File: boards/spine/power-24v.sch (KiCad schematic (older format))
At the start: 0 parts

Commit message: Power management and such
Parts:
- added C72: 0.1uF, 0805, symbol C
- added C73: 1uF, 0805, symbol C
- added CON1: 5-24V 5A, symbol BARREL_JACK
- added CON2: 5-24V 16A, symbol CONN_01X04
- added D8: 8.5VWM, symbol D_Schottky_x2_ACom_KKA
- added Q4: AOD4189, TO-252, symbol Q_PMOS_GDS
- added R33: 100k, symbol R
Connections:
- new net: C72.2, CON1.1, CON2.1 (P1), CON2.2 (P2), Q4.2 (D)
- new net: D8.3 (A), Q4.1 (G), R33.1
- new net +24V: C73.1, D8.1 (K), D8.2 (K), Q4.3 (S)
- new net GND: C72.1, C73.2, CON1.2, CON1.3, CON2.3 (P3), CON2.4 (P4), R33.2
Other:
- note added: "Power input options"
- note added: "Reverse polarity protection"
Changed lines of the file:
@@
 Comment4 ""
 $EndDescr
+$Comp
+L +24V #PWR0138
+U 1 1 564D5D45
+P 7550 3250
+F 0 "#PWR0138" H 7550 3100 50  0001 C CNN
+F 1 "+24V" H 7550 3390 50  0000 C CNN
+F 2 "" H 7550 3250 60  0000 C CNN
+F 3 "" H 7550 3250 60  0000 C CNN
+	1    7550 3250
+	1    0    0    -1
+$EndComp
+$Comp
+L GNDPWR #PWR0139
+U 1 1 564D5D5C
+P 7100 5000
+F 0 "#PWR0139" H 7100 4800 50  0001 C CNN
+F 1 "GNDPWR" H 7100 4870 50  0000 C CNN
+F 2 "" H 7100 4950 60  0000 C CNN
+F 3 "" H 7100 4950 60  0000 C CNN
+	1    7100 5000
+	1    0    0    -1
+$EndComp
+$Comp
+L C C73
+U 1 1 564D690E
+P 7550 4100
+F 0 "C73" H 7600 4200 50  0000 L CNN
+F 1 "1uF " H 7600 4000 50  0000 L CNN
+F 2 "0805" H 7588 3950 30  0001 C CNN
+F 3 "http://www.murata.com/~/media/webrenewal/support/library/catalog/products/capacitor/mlcc/c02e.ashx" H 7550 4100 60  0001 C CNN
+F 4 "GRM219R61H105KA73D" H 7600 3900 39  0001 L BNN "MfgId"
+F 5 "Murata" H 7550 4100 60  0001 C CNN "MfrId"
+F 6 "Digikey" H 7550 4100 60  0001 C CNN "Vend1"
+F 7 "490-10743-2-ND" H 7550 4100 60  0001 C CNN "Vend1Id"
+F 8 "0.03980" H 7550 4100 60  0001 C CNN "RefPrice1k"
+	1    7550 4100
+	1    0    0    -1
+$EndComp
+$Comp
+L GND #PWR0140
+U 1 1 564D690F
+P 7550 5000
+F 0 "#PWR0140" H 7550 4750 50  0001 C CNN
+F 1 "GND" H 7550 4850 50  0000 C CNN
+F 2 "" H 7550 5000 60  0000 C CNN
+F 3 "" H 7550 5000 60  0000 C CNN
+	1    7550 5000
+	1    0    0    -1
+$EndComp
+$Comp
+L BARREL_JACK CON1
+U 1 1 564D6BF2
+P 3950 4050
+F 0 "CON1" H 3950 4300 60  0000 C CNN
+F 1 "5-24V 5A" H 3950 3850 60  0000 C CNN
+F 2 "" H 3950 4050 60  0000 C CNN
+F 3 "http://katalog.we-online.de/em/datasheet/6941xx105102.pdf" H 3950 4050 60  0001 C CNN
+F 4 "Digikey" H 3950 4050 60  0001 C CNN "Vend1"
+F 5 "732-5932-1-ND" H 3950 4050 60  0001 C CNN "Vend1Id"
+F 6 "Wurth" H 3950 4050 60  0001 C CNN "MfrId"
+F 7 "694108105102" H 3950 4050 60  0001 C CNN "MfgId"
+F 8 "1.13" H 3950 4050 60  0001 C CNN "RefPrice1k"
+	1    3950 4050
+	1    0    0    -1
+$EndComp
+$Comp
+L Q_PMOS_GDS Q4
+U 1 1 564D73AF
+P 6050 3500
+F 0 "Q4" V 6300 3750 50  0000 R CNN
+F 1 "AOD4189" V 6300 3550 50  0000 R CNN
+F 2 "TO-252" H 6250 3600 29  0001 C CNN
+F 3 "http://aosmd.com/res/data_sheets/AOD4189.pdf" H 6050 3500 60  0001 C CNN
+F 4 "Digikey" H 6050 3500 60  0001 C CNN "Vend1"
+F 5 "785-1351-1-ND" H 6050 3500 60  0001 C CNN "Vend1Id"
+F 6 "Alpha & Omega" H 6050 3500 60  0001 C CNN "MfgId"
+F 7 "AOD4189" H 6050 3500 60  0001 C CNN "MfrId"
+F 8 "0.196" H 6050 3500 60  0001 C CNN "RefPrice1k"
+	1    6050 3500
+	0    -1   -1   0
+$EndComp
+Wire Wire Line
+	4550 3400 5850 3400
+$Comp
+L C C72
+U 1 1 564D7783
+P 5700 4100
+F 0 "C72" V 5750 3900 50  0000 L CNN
+F 1 "0.1uF" V 5750 4200 50  0000 L CNN
+F 2 "0805" H 5738 3950 30  0001 C CNN
+F 3 "http://psearch.murata.com/capacitor/product/GRM21BR71H104MA01%23.pdf" H 5700 4100 60  0001 C CNN
+F 4 "0.01880" V 5700 4100 60  0001 C CNN "RefPrice1k"
+F 5 "490-9672-2-ND" V 5700 4100 60  0001 C CNN "Vend1Id"
+F 6 "Digikey" V 5700 4100 60  0001 C CNN "Vend1"
+F 7 "Murata" V 5700 4100 60  0001 C CNN "MfrId"
+F 8 "GRM21BR71H104MA01L" V 5700 4100 60  0001 C CNN "MfgId"
+	1    5700 4100
+	-1   0    0    1
+$EndComp
+Wire Wire Line
+	4550 4850 7550 4850
+Wire Wire Line
+	5700 3950 5700 3400
+Connection ~ 5700 3400
+Wire Wire Line
+	5700 4250 5700 4850
+Connection ~ 5700 4850
+$Comp
+L CONN_01X04 CON2
+U 1 1 564D79D9
+P 5150 4100
+F 0 "CON2" H 5150 4350 50  0000 C CNN
+F 1 "5-24V 16A" H 5050 3800 50  0000 C CNN
+F 2 "" H 5150 4100 60  0000 C CNN
+F 3 "http://www.diytrade.com/china/pd/11802786/terminal_block_2EDG_5_08_2P_3P_4P_5P_6P_7P_8P_9P_10P_11P_12P_13P_14P.html" H 5150 4100 60  0001 C CNN
+F 4 "eBay" H 5150 4100 60  0001 C CNN "Vend1"
+F 5 "http://www.ebay.com/itm/331290774584" H 5150 4100 60  0001 C CNN "Vend1Id"
+F 6 "0.23" H 5150 4100 60  0001 C CNN "RefPrice1k"
+F 7 "4way 4pin Screw PCB Terminal Block Connector 3.81mm Pitch Pluggable Type" H 5150 4100 60  0001 C CNN "Description"
+F 8 "E-xun" H 5150 4100 60  0001 C CNN "MfrId"
+F 9 "2EDG-3.81" H 5150 4100 60  0001 C CNN "MfgId"
+	1    5150 4100
+	1    0    0    -1
+$EndComp
+Wire Wire Line
+	4250 3950 4950 3950
+Wire Wire Line
+	4950 4050 4850 4050
+Wire Wire Line
+	4850 4050 4850 3950
+Connection ~ 4850 3950
+Wire Wire Line
+	4250 4050 4300 4050
+Wire Wire Line
+	4300 4050 4300 4150
+Wire Wire Line
+	4250 4150 4950 4150
+Connection ~ 4300 4150
+Wire Wire Line
+	4950 4250 4850 4250
+Wire Wire Line
+	4850 4250 4850 4150
+Connection ~ 4850 4150
+Text Notes 6000 2950 0    60   ~ 0
+Reverse polarity protection
+Text Notes 4050 2950 0    60   ~ 0
+Power input options
+$Comp
+L D_Schottky_x2_ACom_KKA D8
+U 1 1 564D8C89
+P 6800 3800
+F 0 "D8" H 7000 4000 50  0000 R CNN
+F 1 "8.5VWM" H 6550 4000 50  0000 L CNN
+F 2 "" H 6800 3800 60  0000 C CNN
+F 3 "http://www.onsemi.com/pub_link/Collateral/MMBZ5V6ALT1-D.PDF" H 6800 3800 60  0001 C CNN
+F 4 "ON Semi" H 6450 3950 39  0001 L BNN "MfrId"
+F 5 "MMBZ12VALT1G" H 6800 3900 39  0000 C CNN "MfgId"
+F 6 "MMBZ12VALT1GOSCT-ND" H 6800 3800 60  0001 C CNN "Vend1Id"
+F 7 ".04471" H 6800 3800 60  0001 C CNN "RefPrice1k"
+F 8 "Digikey" H 6800 3800 60  0001 C CNN "Vend1"
+	1    6800 3800
+	1    0    0    -1
+$EndComp
+$Comp
+L R R33
+U 1 1 564DB940
+P 6050 4400
+F 0 "R33" V 6130 4400 50  0000 C CNN
+F 1 "100k" V 6050 4400 50  0000 C CNN
+F 2 "" V 5980 4400 30  0000 C CNN
+F 3 "https://www.seielect.com/Catalog/SEI-RMCF_RMCP.pdf" H 6050 4400 30  0001 C CNN
+F 4 "Digikey" V 6050 4400 60  0001 C CNN "Vend1"
+F 5 "Stackpole" V 6050 4400 60  0001 C CNN "MfrId"
+F 6 "RMCF0805JT100K" V 6050 4400 60  0001 C CNN "MfgId"
+F 7 "RMCF0805JT100KCT-ND" V 6050 4400 60  0001 C CNN "Vend1Id"
+F 8 "0.00320" V 6050 4400 60  0001 C CNN "RefPrice1k"
+	1    6050 4400
+	1    0    0    -1
+$EndComp
+Connection ~ 6050 4850
+Wire Wire Line
+	4550 3400 4550 3950
+Connection ~ 4550 3950
+Wire Wire Line
+	4550 4150 4550 4850
+Connection ~ 4550 4150
+Wire Wire Line
+	6250 3400 7550 3400
+Wire Wire Line
+	7250 3400 7250 3800
+Wire Wire Line
+	7250 3800 7100 3800
+Wire Wire Line
+	6500 3800 6350 3800
+Wire Wire Line
+	6350 3800 6350 3400
+Connection ~ 6350 3400
+Wire Wire Line
+	6800 4000 6800 4100
+Wire Wire Line
+	6800 4100 6050 4100
+Wire Wire Line
+	6050 3700 6050 4250
+Connection ~ 6050 4100
+Wire Wire Line
+	6050 4550 6050 4850
+Wire Wire Line
+	7550 3250 7550 3950
+Wire Wire Line
+	7550 4250 7550 5000
+Connection ~ 7550 3400
+Connection ~ 7250 3400
+Connection ~ 7550 4850
+Wire Wire Line
+	7100 5000 7100 4850
+Connection ~ 7100 4850
 $EndSCHEMATC

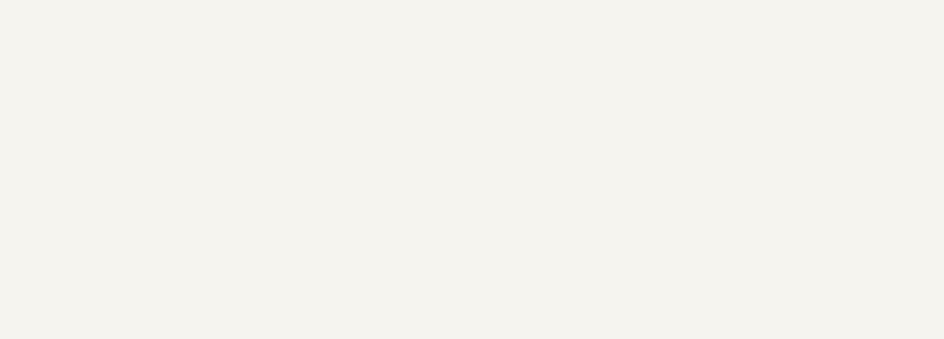
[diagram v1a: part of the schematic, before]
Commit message: Clock generator, sync connectors, title blocks
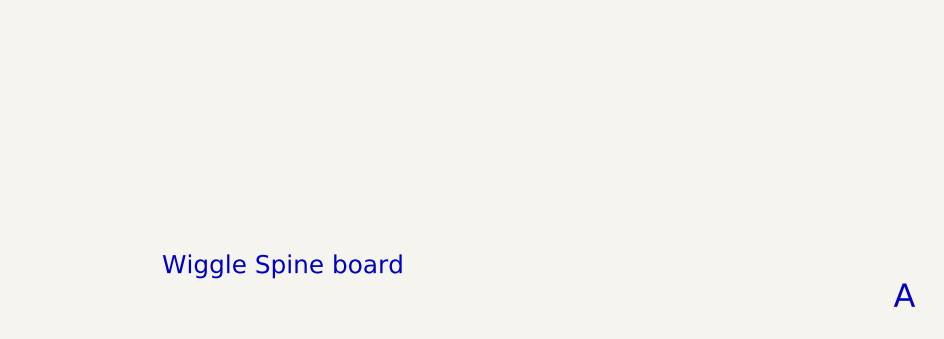
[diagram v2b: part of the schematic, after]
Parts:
- C72, C73: footprint 0805 -> Capacitors_SMD:C_0805
- R33: footprint (none) -> Resistors_SMD:R_0805
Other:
- note added: "A"
- note added: "Wiggle Spine board"

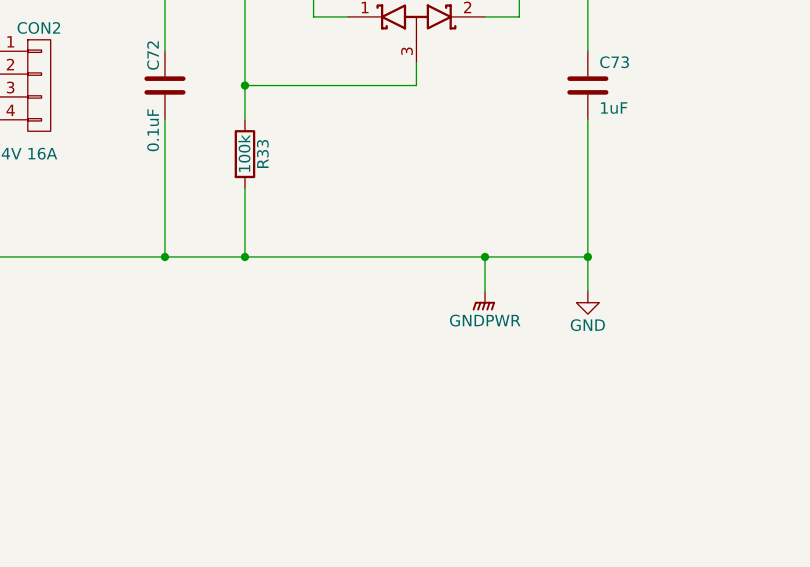
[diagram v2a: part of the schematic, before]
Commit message: Fixes for shield grounds and module numbering
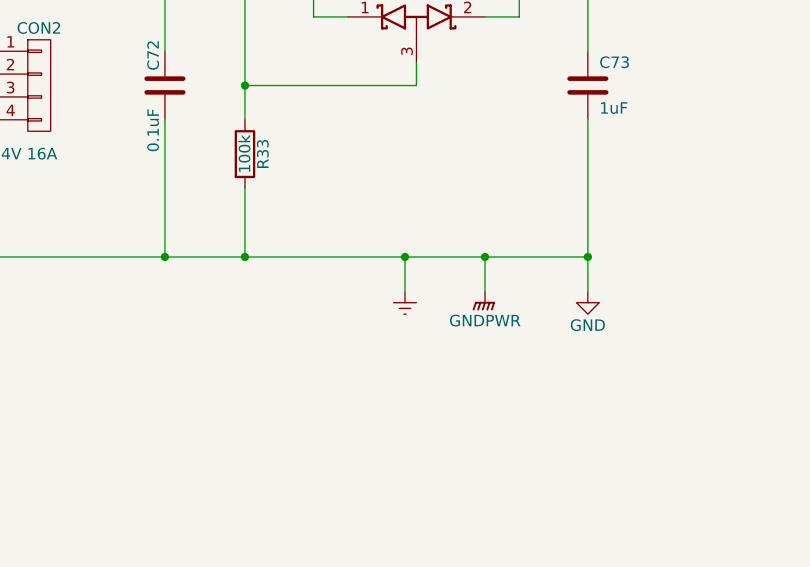
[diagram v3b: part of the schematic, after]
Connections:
- net GND renamed Earth
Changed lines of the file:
@@
 $EndDescr
 $Comp
-L +24V #PWR0138
+L +24V #PWR0139
 U 1 1 564D5D45
 P 7550 3250
-F 0 "#PWR0138" H 7550 3100 50  0001 C CNN
+F 0 "#PWR0139" H 7550 3100 50  0001 C CNN
 F 1 "+24V" H 7550 3390 50  0000 C CNN
 F 2 "" H 7550 3250 60  0000 C CNN
@@
 $EndComp
 $Comp
-L GNDPWR #PWR0139
+L GNDPWR #PWR0140
 U 1 1 564D5D5C
 P 7100 5000
-F 0 "#PWR0139" H 7100 4800 50  0001 C CNN
+F 0 "#PWR0140" H 7100 4800 50  0001 C CNN
 F 1 "GNDPWR" H 7100 4870 50  0000 C CNN
 F 2 "" H 7100 4950 60  0000 C CNN
@@
 $EndComp
 $Comp
-L GND #PWR0140
+L GND #PWR0141
 U 1 1 564D690F
 P 7550 5000
-F 0 "#PWR0140" H 7550 4750 50  0001 C CNN
+F 0 "#PWR0141" H 7550 4750 50  0001 C CNN
 F 1 "GND" H 7550 4850 50  0000 C CNN
 F 2 "" H 7550 5000 60  0000 C CNN
@@
 Text Notes 9900 7900 0    102  ~ 0
 A
+$Comp
+L Earth #PWR0142
+U 1 1 565B7572
+P 6750 5000
+F 0 "#PWR0142" H 6750 4750 50  0001 C CNN
+F 1 "Earth" H 6750 4850 50  0001 C CNN
+F 2 "" H 6750 5000 60  0000 C CNN
+F 3 "" H 6750 5000 60  0000 C CNN
+	1    6750 5000
+	1    0    0    -1
+$EndComp
+Wire Wire Line
+	6750 5000 6750 4850
+Connection ~ 6750 4850
 $EndSCHEMATC

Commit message: Schematic footprint and refdes work
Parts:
- CON1: footprint (none) -> Connect:BARREL_JACK
- CON2: footprint (none) -> Terminal_Blocks:TerminalBlock_Pheonix_PT-3.5mm_4pol
- D8: footprint (none) -> TO_SOT_Packages_SMD:SOT-23
- Q4: footprint TO-252 -> TO_SOT_Packages_SMD:TO-252-2Lead
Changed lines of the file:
@@
 $EndDescr
 $Comp
-L +24V #PWR0139
+L +24V #PWR141
 U 1 1 564D5D45
 P 7550 3250
-F 0 "#PWR0139" H 7550 3100 50  0001 C CNN
+F 0 "#PWR141" H 7550 3100 50  0001 C CNN
 F 1 "+24V" H 7550 3390 50  0000 C CNN
 F 2 "" H 7550 3250 60  0000 C CNN
@@
 $EndComp
 $Comp
-L GNDPWR #PWR0140
+L GNDPWR #PWR140
 U 1 1 564D5D5C
 P 7100 5000
-F 0 "#PWR0140" H 7100 4800 50  0001 C CNN
+F 0 "#PWR140" H 7100 4800 50  0001 C CNN
 F 1 "GNDPWR" H 7100 4870 50  0000 C CNN
 F 2 "" H 7100 4950 60  0000 C CNN
@@
 $EndComp
 $Comp
-L GND #PWR0141
+L GND #PWR142
 U 1 1 564D690F
 P 7550 5000
-F 0 "#PWR0141" H 7550 4750 50  0001 C CNN
+F 0 "#PWR142" H 7550 4750 50  0001 C CNN
 F 1 "GND" H 7550 4850 50  0000 C CNN
 F 2 "" H 7550 5000 60  0000 C CNN
@@
 F 0 "CON1" H 3950 4300 60  0000 C CNN
 F 1 "5-24V 5A" H 3950 3850 60  0000 C CNN
-F 2 "" H 3950 4050 60  0001 C CNN
+F 2 "Connect:BARREL_JACK" H 3950 4050 60  0001 C CNN
 F 3 "http://katalog.we-online.de/em/datasheet/6941xx105102.pdf" H 3950 4050 60  0001 C CNN
 F 4 "Digikey" H 3950 4050 60  0001 C CNN "Vend1"
@@
 F 0 "Q4" V 6300 3750 50  0000 R CNN
 F 1 "AOD4189" V 6300 3550 50  0000 R CNN
-F 2 "TO-252" H 6250 3600 29  0001 C CNN
+F 2 "TO_SOT_Packages_SMD:TO-252-2Lead" H 6250 3600 29  0001 C CNN
 F 3 "http://aosmd.com/res/data_sheets/AOD4189.pdf" H 6050 3500 60  0001 C CNN
 F 4 "Digikey" H 6050 3500 60  0001 C CNN "Vend1"
@@
 F 0 "CON2" H 5150 4350 50  0000 C CNN
 F 1 "5-24V 16A" H 5050 3800 50  0000 C CNN
-F 2 "" H 5150 4100 60  0001 C CNN
+F 2 "Terminal_Blocks:TerminalBlock_Pheonix_PT-3.5mm_4pol" H 5150 4100 60  0001 C CNN
 F 3 "http://www.diytrade.com/china/pd/11802786/terminal_block_2EDG_5_08_2P_3P_4P_5P_6P_7P_8P_9P_10P_11P_12P_13P_14P.html" H 5150 4100 60  0001 C CNN
 F 4 "eBay" H 5150 4100 60  0001 C CNN "Vend1"
@@
 F 0 "D8" H 7000 4000 50  0000 R CNN
 F 1 "8.5VWM" H 6550 4000 50  0000 L CNN
-F 2 "" H 6800 3800 60  0001 C CNN
+F 2 "TO_SOT_Packages_SMD:SOT-23" H 6800 3800 60  0001 C CNN
 F 3 "http://www.onsemi.com/pub_link/Collateral/MMBZ5V6ALT1-D.PDF" H 6800 3800 60  0001 C CNN
 F 4 "ON Semi" H 6450 3950 39  0001 L BNN "MfrId"
@@
 A
 $Comp
-L Earth #PWR0142
+L Earth #PWR139
 U 1 1 565B7572
 P 6750 5000
-F 0 "#PWR0142" H 6750 4750 50  0001 C CNN
+F 0 "#PWR139" H 6750 4750 50  0001 C CNN
 F 1 "Earth" H 6750 4850 50  0001 C CNN
 F 2 "" H 6750 5000 60  0000 C CNN

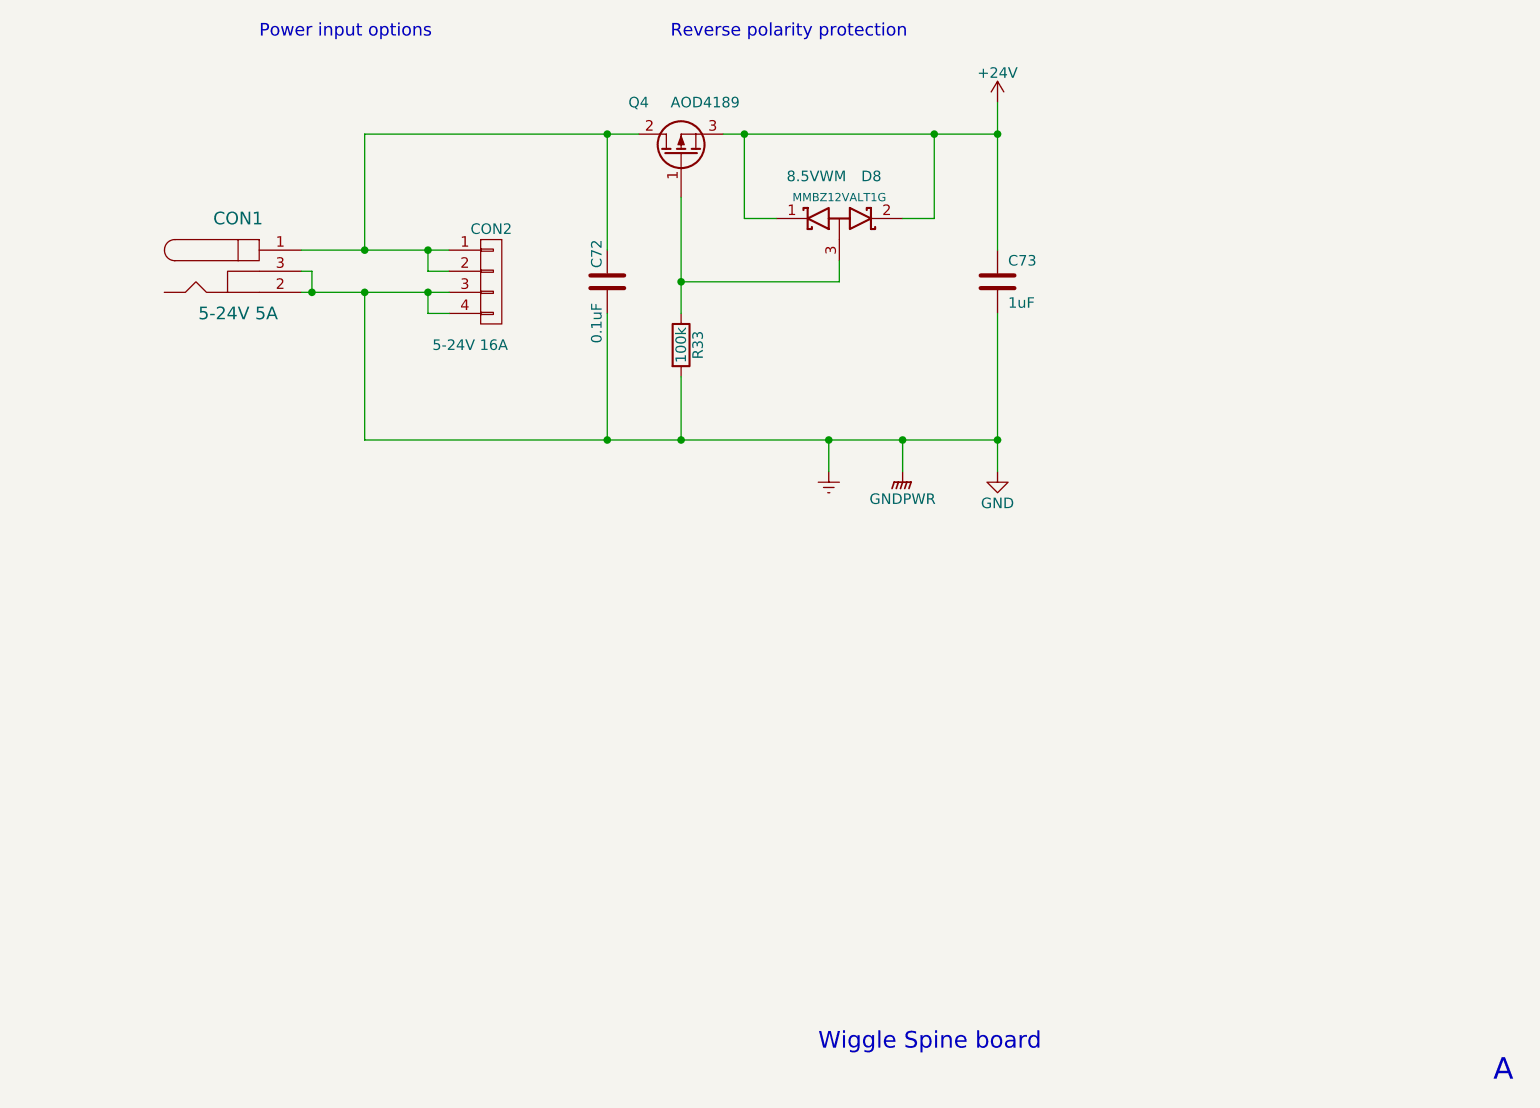
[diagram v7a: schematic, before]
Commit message: Separated ground planes, starting on design rules
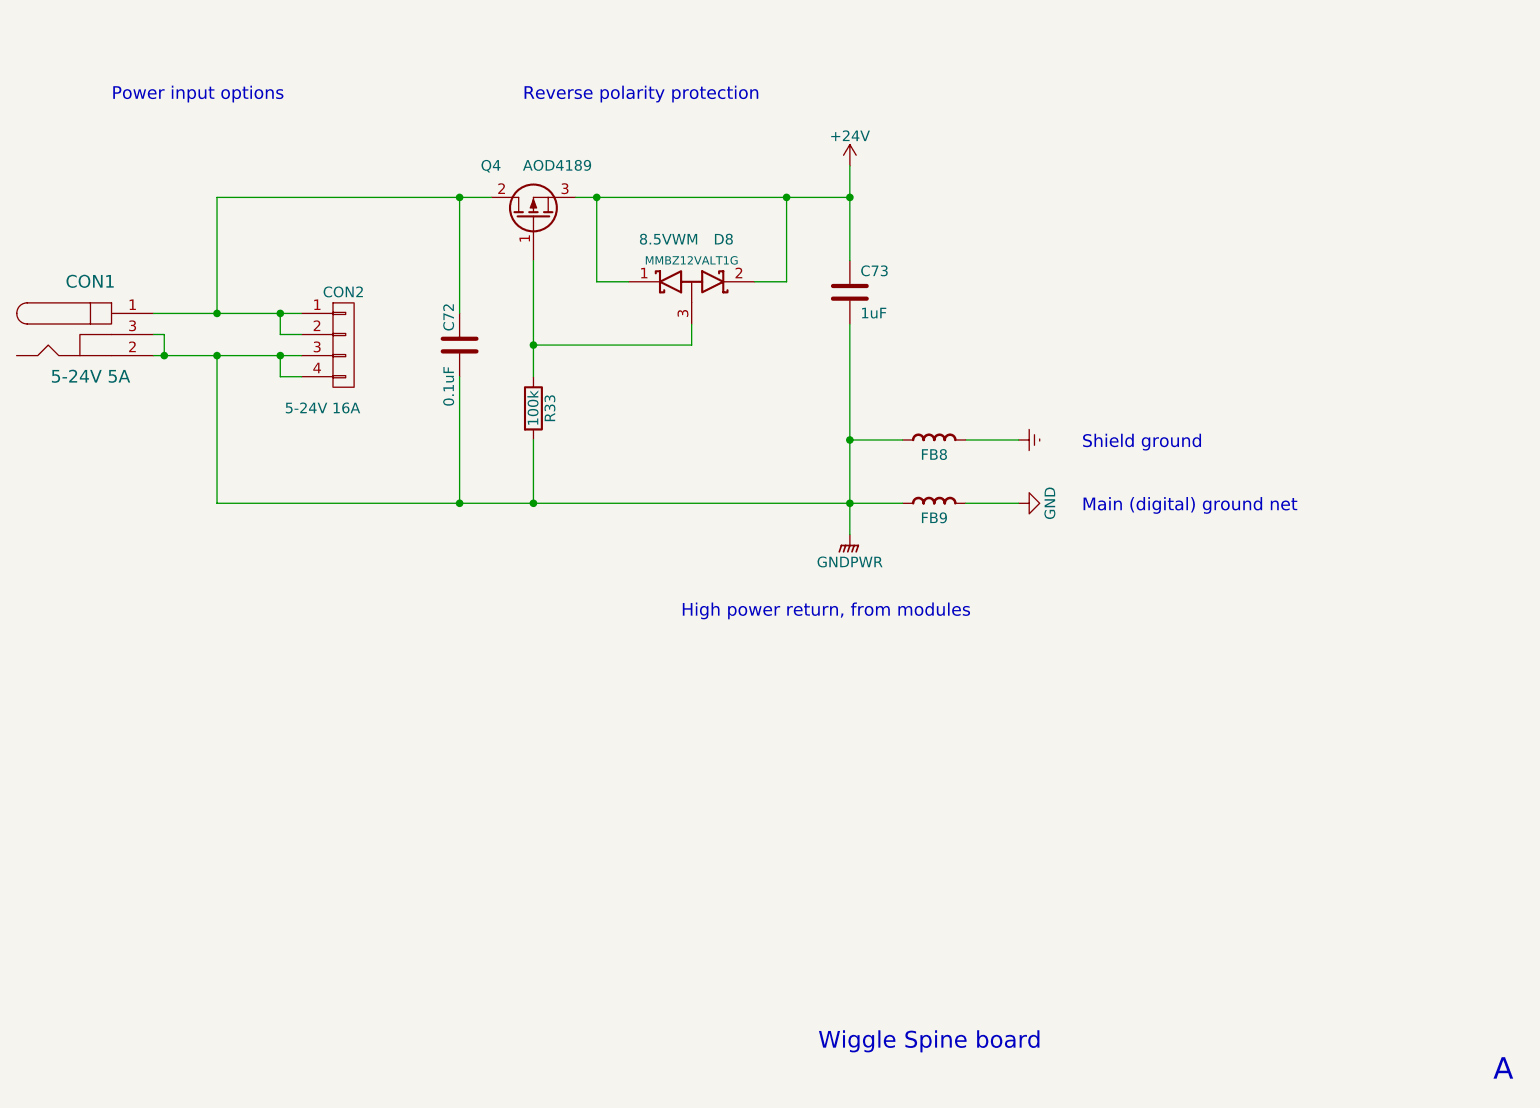
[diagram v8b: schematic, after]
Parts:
- added FB8, FB9: Ferrite bead, Resistors_SMD:R_0805, symbol FERRITE_BEAD
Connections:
- net Earth: now also FB8.2; no longer C72.1, C73.2, CON1.2, CON1.3, CON2.3 (P3), CON2.4 (P4), R33.2
- new net GND: FB9.2
- new net GNDPWR: C72.1, C73.2, CON1.2, CON1.3, CON2.3 (P3), CON2.4 (P4), FB8.1, FB9.1, R33.2
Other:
- note added: "High power return, from modules"
- note added: "Main (digital) ground net"
- note added: "Shield ground"
- moved on the sheet: C72, C73, CON1, CON2, D8, Q4, R33
